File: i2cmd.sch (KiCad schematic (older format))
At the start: 15 parts

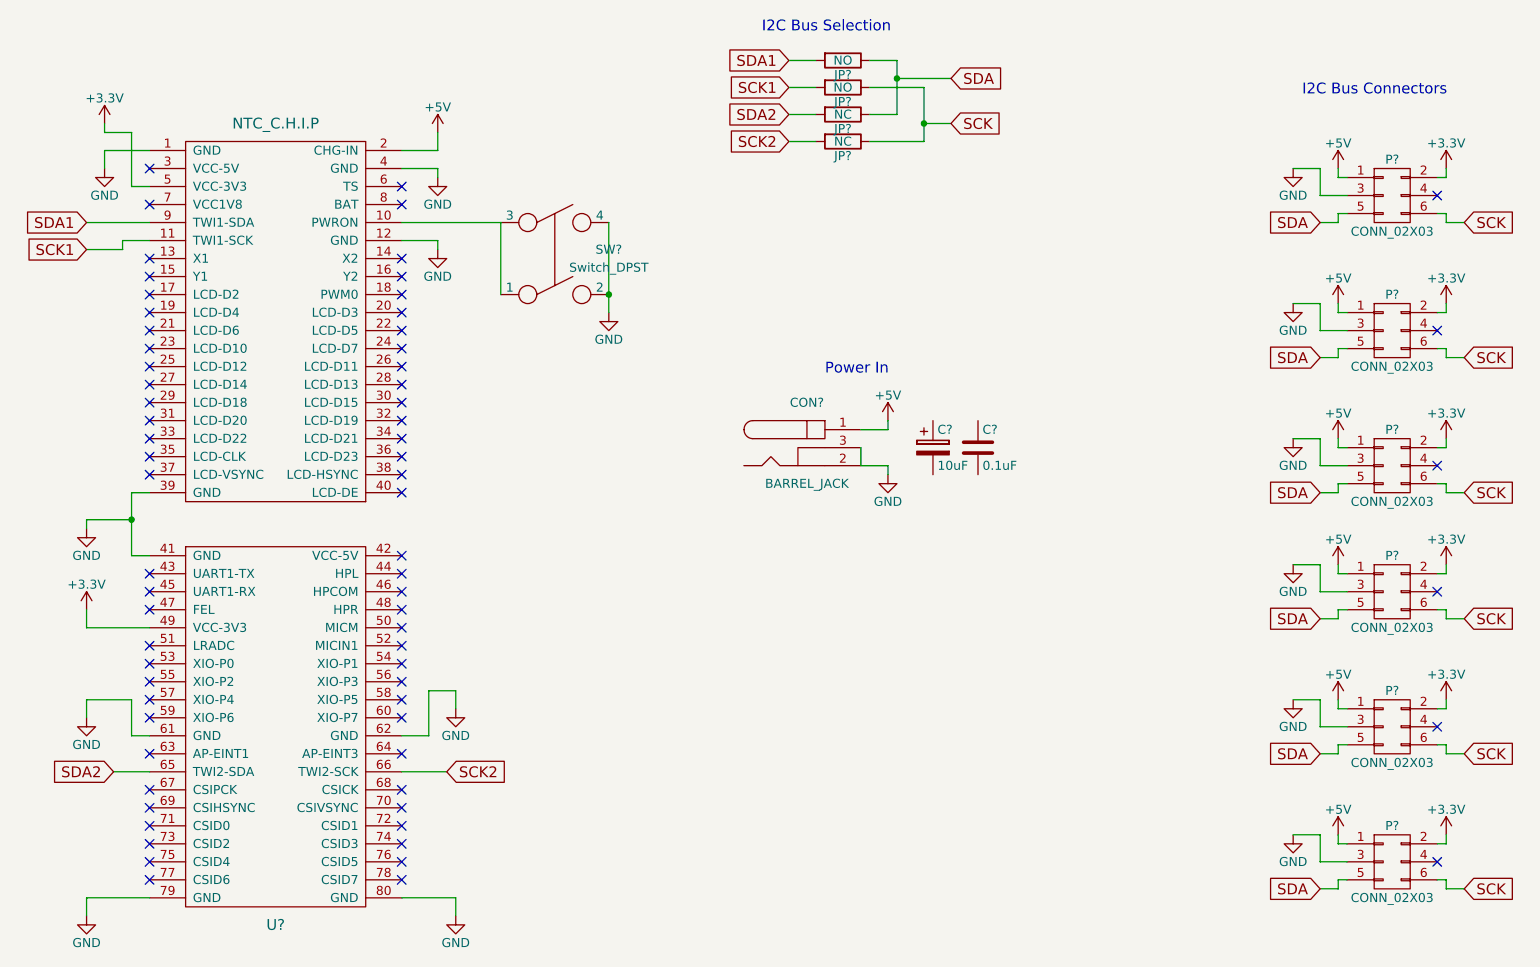
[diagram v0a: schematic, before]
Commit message: Added netlist and base footprints.
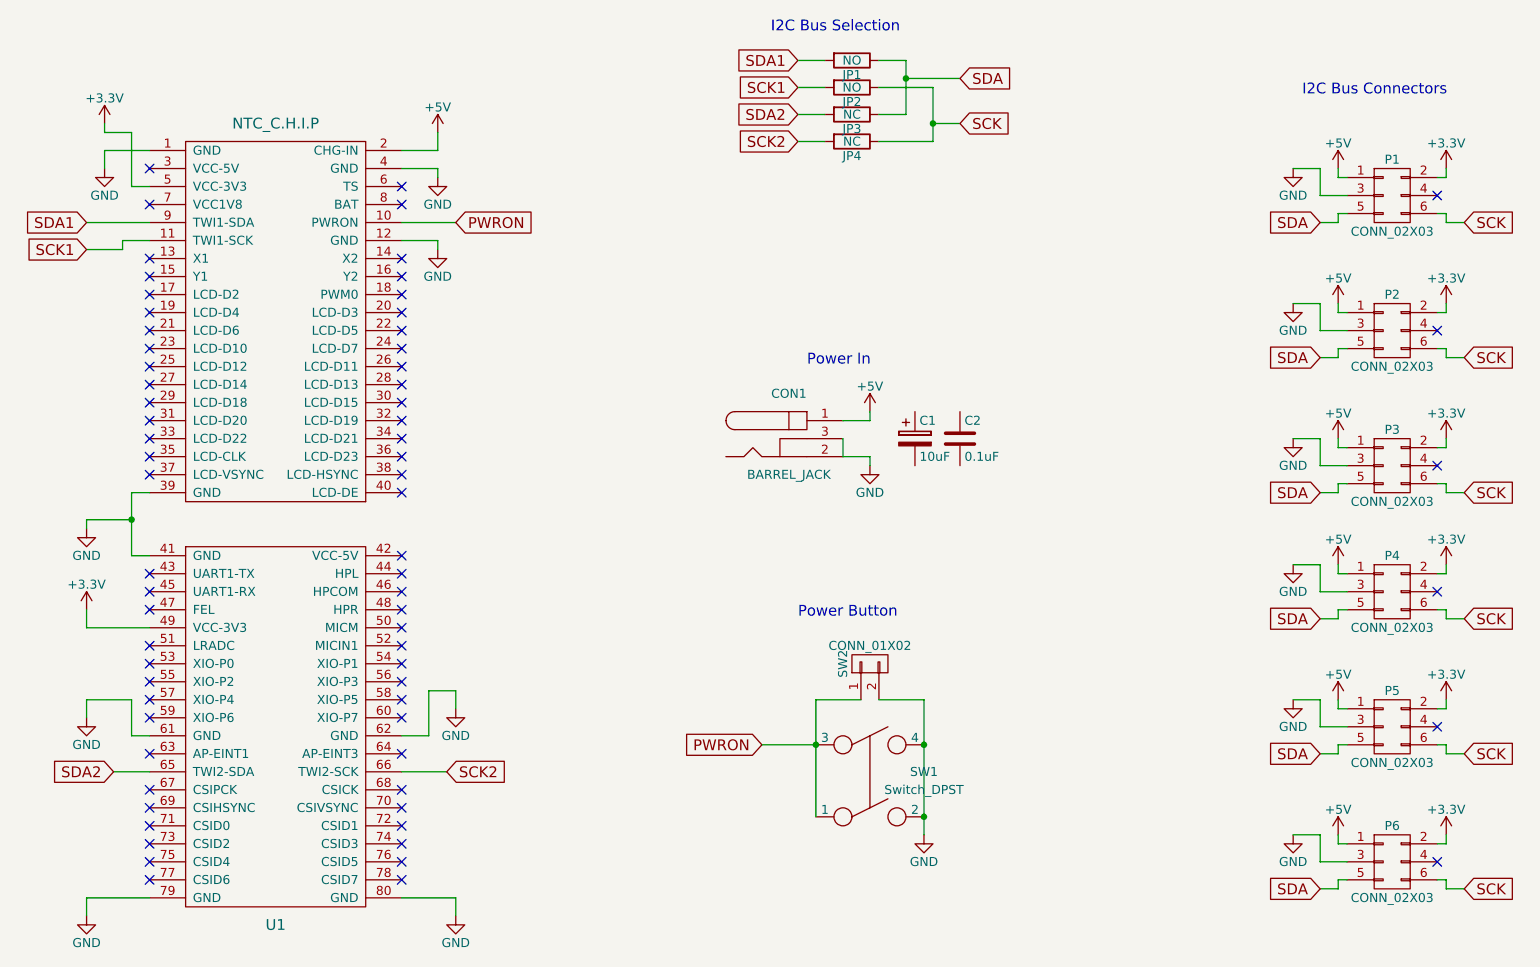
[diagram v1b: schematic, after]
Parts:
- added SW2: CONN_01X02, Pin_Headers:Pin_Header_Straight_1x02, symbol CONN_01X02
- C1: renamed from C?; footprint (none) -> Capacitors_ThroughHole:C_Radial_D5_L6_P2.5
- C2: renamed from C?; footprint (none) -> Capacitors_ThroughHole:C_Disc_D3_P2.5
- CON1: renamed from CON?; footprint (none) -> Connect:BARREL_JACK
- JP1: renamed from JP?; footprint (none) -> Resistors_SMD:R_0201
- JP2, JP3, JP4: renamed from R?; footprint (none) -> Resistors_SMD:R_0201
- P1, P2, P3, P4, P5, P6: renamed from P?; footprint (none) -> Pin_Headers:Pin_Header_Straight_2x06
- SW1: renamed from SW?; footprint (none) -> Buttons_Switches_ThroughHole:SW_PUSH_SMALL
- U1: renamed from U?; footprint (none) -> ntc-chip:ntc_chip
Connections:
- net GND: now also SW2.2 (P2)
- net PWRON: now reaches SW1.1, SW1.3, U1.10 (PWRON)
- net PWRON: now also SW2.1 (P1)
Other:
- note added: "Power Button"
- moved on the sheet: C1, C2, CON1, JP1, JP2, JP3, JP4, SW1

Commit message: Added initial version of the board.
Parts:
- P1, P2, P3, P4, P5, P6: footprint Pin_Headers:Pin_Header_Straight_2x06 -> Pin_Headers:Pin_Header_Straight_2x03
- SW1: footprint Buttons_Switches_ThroughHole:SW_PUSH_SMALL -> libs:sw_push_small
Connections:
- net +5V: now also C1.1, C2.1
- net GND: now also C1.2, C2.2
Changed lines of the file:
@@
 F 0 "P1" H 9200 2200 50  0000 C CNN
 F 1 "CONN_02X03" H 9200 1800 50  0000 C CNN
-F 2 "Pin_Headers:Pin_Header_Straight_2x06" H 9200 800 50  0001 C CNN
+F 2 "Pin_Headers:Pin_Header_Straight_2x03" H 9200 800 50  0001 C CNN
 F 3 "" H 9200 800 50  0000 C CNN
 	1    9200 2000
@@
 F 0 "SW1" H 6600 5300 50  0000 C CNN
 F 1 "Switch_DPST" H 6600 5200 50  0000 C CNN
-F 2 "Buttons_Switches_ThroughHole:SW_PUSH_SMALL" H 6300 5250 50  0001 C CNN
+F 2 "libs:sw_push_small" H 6300 5250 50  0001 C CNN
 F 3 "" H 6300 5250 50  0000 C CNN
 	1    6300 5250
@@
 Connection ~ 6600 5450
 Wire Wire Line
-	6150 3250 6300 3250
+	6150 3250 6400 3250
 Wire Wire Line
 	6300 3250 6300 3200
@@
 	6150 3350 6150 3450
 Wire Wire Line
-	6150 3450 6300 3450
+	6150 3450 6400 3450
 Wire Wire Line
 	6300 3450 6300 3500
@@
 F 0 "P2" H 9200 2950 50  0000 C CNN
 F 1 "CONN_02X03" H 9200 2550 50  0000 C CNN
-F 2 "Pin_Headers:Pin_Header_Straight_2x06" H 9200 1550 50  0001 C CNN
+F 2 "Pin_Headers:Pin_Header_Straight_2x03" H 9200 1550 50  0001 C CNN
 F 3 "" H 9200 1550 50  0000 C CNN
 	1    9200 2750
@@
 F 0 "P3" H 9200 3700 50  0000 C CNN
 F 1 "CONN_02X03" H 9200 3300 50  0000 C CNN
-F 2 "Pin_Headers:Pin_Header_Straight_2x06" H 9200 2300 50  0001 C CNN
+F 2 "Pin_Headers:Pin_Header_Straight_2x03" H 9200 2300 50  0001 C CNN
 F 3 "" H 9200 2300 50  0000 C CNN
 	1    9200 3500
@@
 F 0 "P4" H 9200 4400 50  0000 C CNN
 F 1 "CONN_02X03" H 9200 4000 50  0000 C CNN
-F 2 "Pin_Headers:Pin_Header_Straight_2x06" H 9200 3000 50  0001 C CNN
+F 2 "Pin_Headers:Pin_Header_Straight_2x03" H 9200 3000 50  0001 C CNN
 F 3 "" H 9200 3000 50  0000 C CNN
 	1    9200 4200
@@
 F 0 "P5" H 9200 5150 50  0000 C CNN
 F 1 "CONN_02X03" H 9200 4750 50  0000 C CNN
-F 2 "Pin_Headers:Pin_Header_Straight_2x06" H 9200 3750 50  0001 C CNN
+F 2 "Pin_Headers:Pin_Header_Straight_2x03" H 9200 3750 50  0001 C CNN
 F 3 "" H 9200 3750 50  0000 C CNN
 	1    9200 4950
@@
 F 0 "P6" H 9200 5900 50  0000 C CNN
 F 1 "CONN_02X03" H 9200 5500 50  0000 C CNN
-F 2 "Pin_Headers:Pin_Header_Straight_2x06" H 9200 4500 50  0001 C CNN
+F 2 "Pin_Headers:Pin_Header_Straight_2x03" H 9200 4500 50  0001 C CNN
 F 3 "" H 9200 4500 50  0000 C CNN
 	1    9200 5700
@@
 Text Notes 5900 4350 0    60   ~ 0
 Power Button
+Wire Wire Line
+	6400 3200 6800 3200
+Wire Wire Line
+	6400 3250 6400 3200
+Connection ~ 6300 3250
+Connection ~ 6550 3200
+Wire Wire Line
+	6400 3500 6800 3500
+Wire Wire Line
+	6400 3450 6400 3500
+Connection ~ 6300 3450
+Connection ~ 6550 3500
 $EndSCHEMATC
